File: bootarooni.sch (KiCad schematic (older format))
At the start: 25 parts, among them J1 USB_B_Micro, U1 74LS05, U2 Pico_USB, U3 ADUM3160, U4 74LCX541, U5 74AHCT1G125, U6 74LS299, U7 74LS299, U8 74LS299

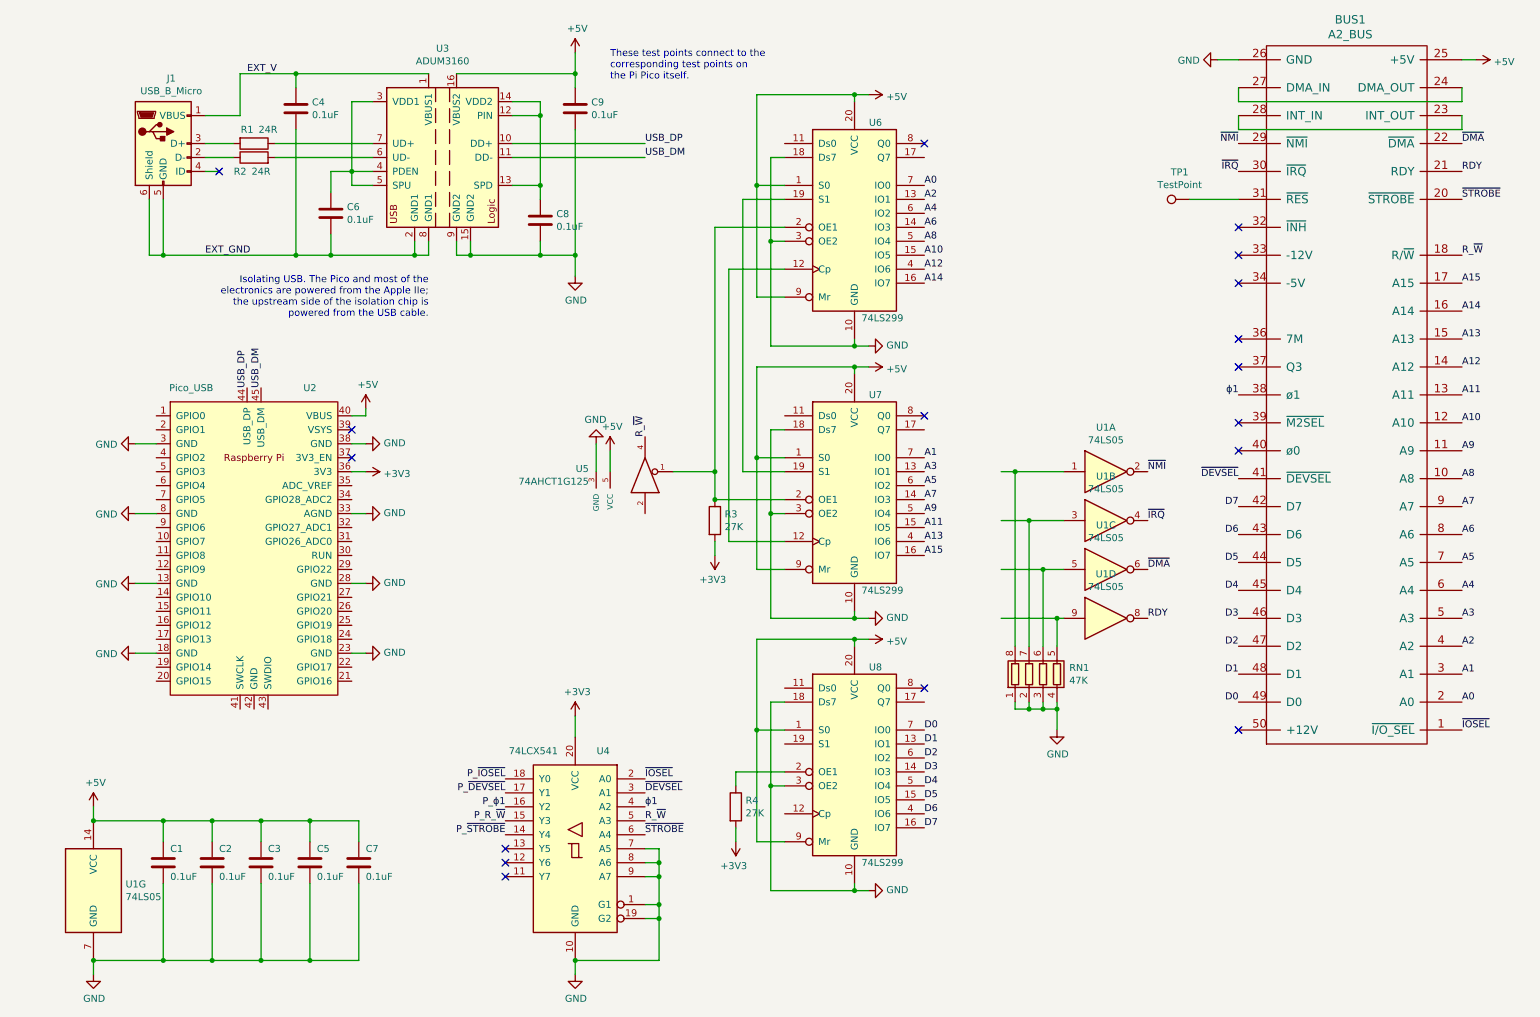
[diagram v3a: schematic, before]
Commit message: added LEDs, most layout done, need to reroute the power line
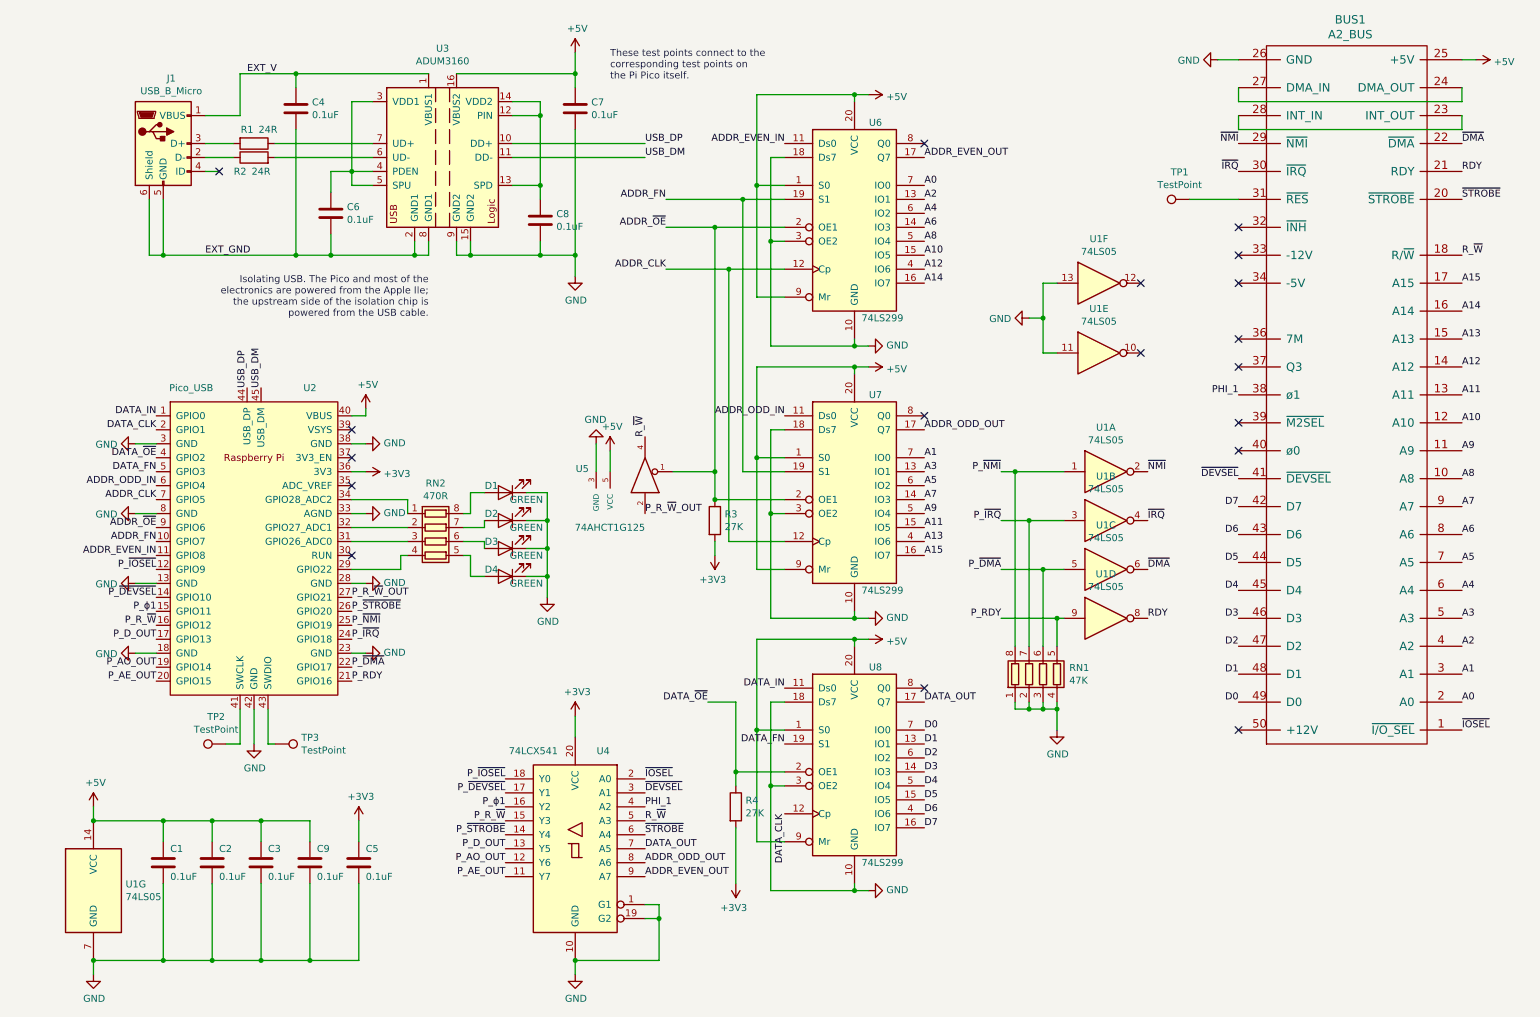
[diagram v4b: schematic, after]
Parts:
- added D1, D2, D3, D4: GREEN, LED_SMD:LED_0805_2012Metric, symbol Device:LED
- added RN2: 470R, bootarooni:SOIC-8, symbol Device:R_Pack04
- added TP2, TP3: TestPoint, TestPoint:TestPoint_Pad_D1.5mm, symbol Connector:TestPoint
- added unit 5 of U1
- added unit 6 of U1
- renumbered C9 to C7, C7 to C9
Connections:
- net +3V3: now also C5.2
- net +5V: no longer C5.2
- net GND: now also U2.42 (GND), D1.1 (K), D2.1 (K), D3.1 (K), D4.1 (K), U1.11, U1.13; no longer U4.7 (A5), U4.8 (A6), U4.9 (A7)
- net P_R_~W~: now also U2.16 (GPIO12)
- net P_~DEVSEL~: now also U2.14 (GPIO10)
- net P_~IOSEL~: now also U2.12 (GPIO9)
- net P_~STROBE~: now also U2.26 (GPIO20)
- net P_ϕ1: now also U2.15 (GPIO11)
- net ADDR_EVEN_IN: now reaches U6.11 (Ds0)
- net ADDR_EVEN_IN: now also U2.11 (GPIO8)
- net ADDR_CLK: now reaches U6.12 (Cp), U7.12 (Cp)
- net ADDR_CLK: now also U2.7 (GPIO5)
- net ADDR_EVEN_OUT: now reaches U6.17 (Q7)
- net ADDR_EVEN_OUT: now also U4.9 (A7)
- net ADDR_FN: now reaches U6.19 (S1), U7.19 (S1)
- net ADDR_FN: now also U2.10 (GPIO7)
- net ADDR_~OE~: now reaches R3.1, U5.1, U6.2 (OE1), U7.2 (OE1)
- net ADDR_~OE~: now also U2.9 (GPIO6)
- net P_AE_OUT: now reaches U4.11 (Y7)
- net P_AE_OUT: now also U2.20 (GPIO15)
- net P_AO_OUT: now reaches U4.12 (Y6)
- net P_AO_OUT: now also U2.19 (GPIO14)
- net P_D_OUT: now reaches U4.13 (Y5)
- net P_D_OUT: now also U2.17 (GPIO13)
- net P_R_~W~_OUT: now reaches U5.2
- net P_R_~W~_OUT: now also U2.27 (GPIO21)
- net ADDR_ODD_IN: now reaches U7.11 (Ds0)
- net ADDR_ODD_IN: now also U2.6 (GPIO4)
- net ADDR_ODD_OUT: now reaches U7.17 (Q7)
- net ADDR_ODD_OUT: now also U4.8 (A6)
- net DATA_IN: now reaches U8.11 (Ds0)
- net DATA_IN: now also U2.1 (GPIO0)
- net DATA_CLK: now reaches U8.12 (Cp)
- net DATA_CLK: now also U2.2 (GPIO1)
- net DATA_OUT: now reaches U8.17 (Q7)
- net DATA_OUT: now also U4.7 (A5)
- net DATA_FN: now reaches U8.19 (S1)
- net DATA_FN: now also U2.5 (GPIO3)
- net DATA_~OE~: now reaches R4.1, U8.2 (OE1)
- net DATA_~OE~: now also U2.4 (GPIO2)
- net P_RDY: now reaches U2.21 (GPIO16)
- net P_RDY: now also RN1.5 (R4.2), U1.9
- net P_~DMA~: now reaches U2.22 (GPIO17)
- net P_~DMA~: now also RN1.6 (R3.2), U1.5
- net P_~IRQ~: now reaches U2.24 (GPIO18)
- net P_~IRQ~: now also RN1.7 (R2.2), U1.3
- net P_~NMI~: now reaches U2.25 (GPIO19)
- net P_~NMI~: now also RN1.8 (R1.2), U1.1
- net at U2.29 (GPIO22): now also RN2.4 (R4.1)
- net at U2.31 (GPIO26_ADC0): now also RN2.3 (R3.1)
- net at U2.32 (GPIO27_ADC1): now also RN2.2 (R2.1)
- net at U2.34 (GPIO28_ADC2): now also RN2.1 (R1.1)
- net at U2.41 (SWCLK): now also TP2.1
- net at U2.43 (SWDIO): now also TP3.1
- net ϕ1 renamed PHI_1
- new net: D4.2 (A), RN2.5 (R4.2)
- new net: D3.2 (A), RN2.6 (R3.2)
- new net: D2.2 (A), RN2.7 (R2.2)
- new net: D1.2 (A), RN2.8 (R1.2)
- no-connect marks 17 -> 18
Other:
- moved on the sheet: C5, C9

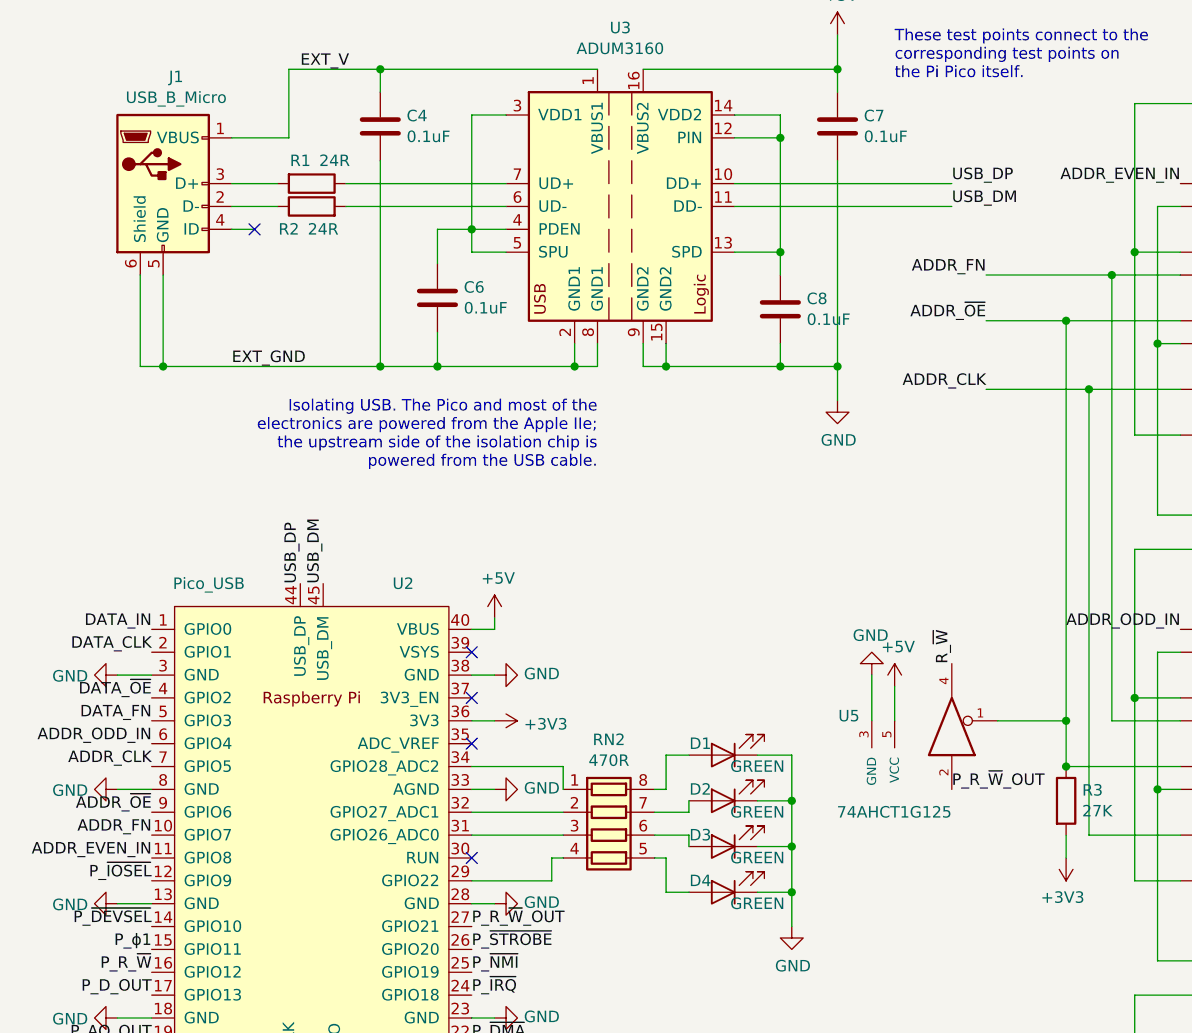
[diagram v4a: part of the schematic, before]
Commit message: initial layout done, needs board edge and mounting holes, along with verification
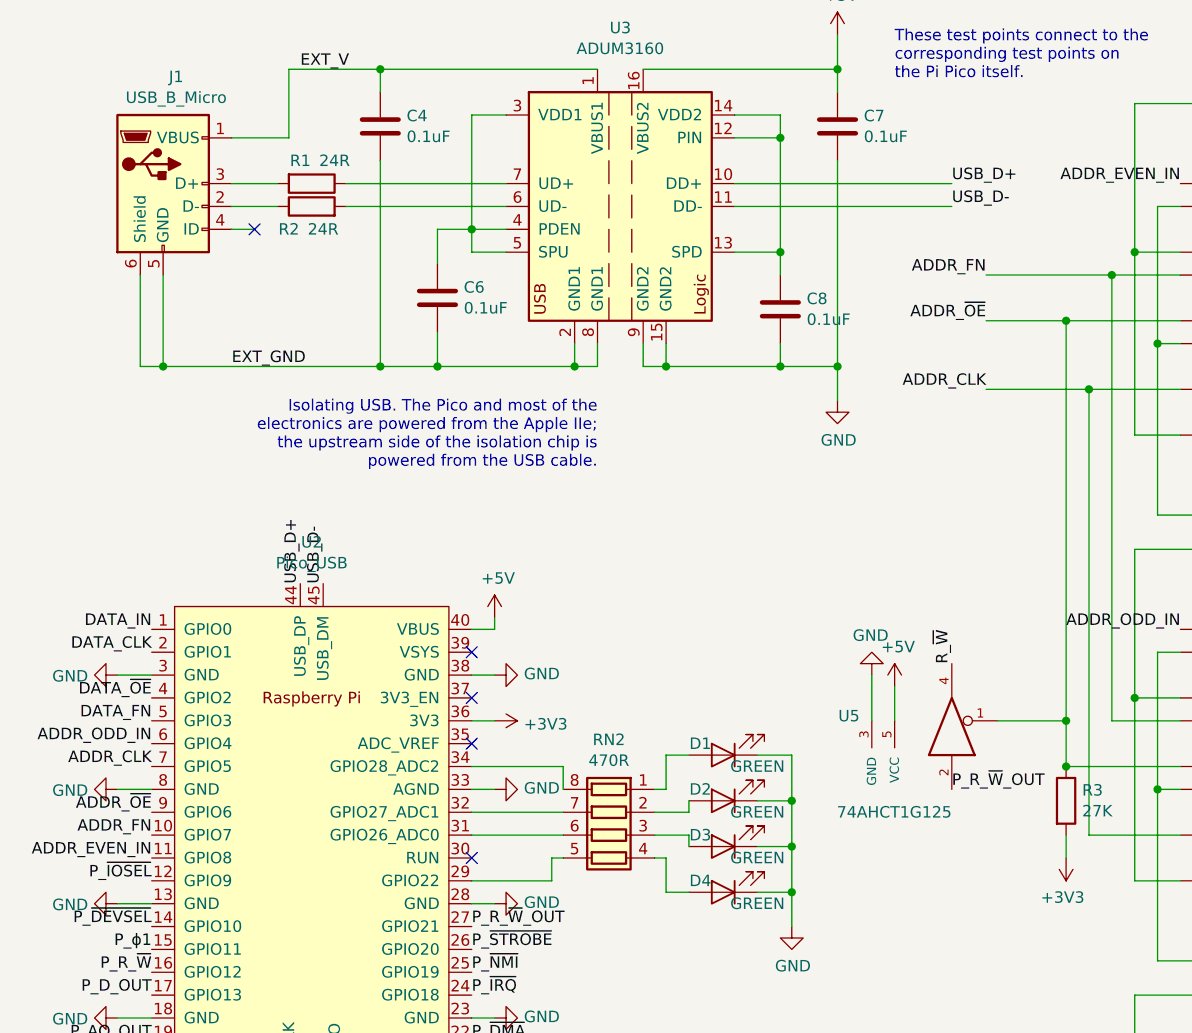
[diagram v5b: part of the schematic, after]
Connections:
- net at RN2.4 (R4.1): now also D4.2 (A); no longer U2.29 (GPIO22)
- net at RN2.3 (R3.1): now also D3.2 (A); no longer U2.31 (GPIO26_ADC0)
- net at RN2.2 (R2.1): now also D2.2 (A); no longer U2.32 (GPIO27_ADC1)
- net at RN2.1 (R1.1): now also D1.2 (A); no longer U2.34 (GPIO28_ADC2)
- net at RN2.5 (R4.2): now also U2.29 (GPIO22); no longer D4.2 (A)
- net at RN2.6 (R3.2): now also U2.31 (GPIO26_ADC0); no longer D3.2 (A)
- net at RN2.7 (R2.2): now also U2.32 (GPIO27_ADC1); no longer D2.2 (A)
- net at RN2.8 (R1.2): now also U2.34 (GPIO28_ADC2); no longer D1.2 (A)
- net USB_DM renamed USB_D-
- net USB_DP renamed USB_D+
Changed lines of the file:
@@
 NoConn ~ 1750 1750
 Text Label 4800 1550 0    50   ~ 0
-USB_DP
+USB_D+
 Text Label 4800 1650 0    50   ~ 0
-USB_DM
+USB_D-
 $Comp
 L power:GND #PWR0101
@@
 Wire Wire Line
 	8700 1950 9050 1950
-$Comp
-L MCU_RaspberryPi_and_Boards:Pico_USB U2
-U 1 1 6040CDC5
-P 2000 4450
-F 0 "U2" H 2400 5600 50  0000 C CNN
-F 1 "Pico_USB" H 1550 5600 50  0000 C CNN
-F 2 "MCU_RaspberryPi_and_Boards:RPi_Pico_USB_SMD_TH" V 2000 4450 50  0001 C CNN
-F 3 "" H 2000 4450 50  0001 C CNN
-	1    2000 4450
-	1    0    0    -1
-$EndComp
 Text Label 1950 3300 1    50   ~ 0
-USB_DP
+USB_D+
 Text Label 2050 3300 1    50   ~ 0
-USB_DM
+USB_D-
 Wire Wire Line
 	9050 1150 9050 1250
@@
 F 3 "~" H 3300 4400 50  0001 C CNN
 	1    3300 4400
-	0    1    1    0
+	0    -1   1    0
 $EndComp
 Wire Wire Line
@@
 	4100 4050 4100 4250
 Connection ~ 4100 4250
+$Comp
+L MCU_RaspberryPi_and_Boards:Pico_USB U2
+U 1 1 608C304D
+P 2000 4450
+F 0 "U2" H 2000 5781 50  0000 C CNN
+F 1 "Pico_USB" H 2000 5690 50  0000 C CNN
+F 2 "MCU_RaspberryPi_and_Boards:RPi_Pico_USB_SMD_TH" V 2000 4450 50  0001 C CNN
+F 3 "" H 2000 4450 50  0001 C CNN
+	1    2000 4450
+	1    0    0    -1
+$EndComp
 $EndSCHEMATC

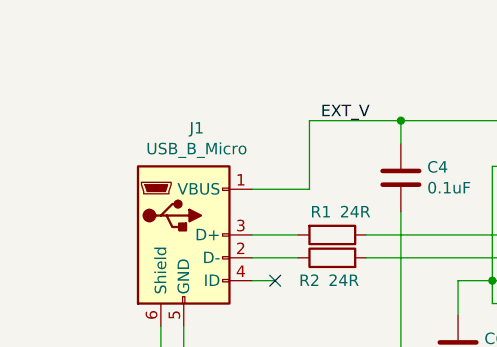
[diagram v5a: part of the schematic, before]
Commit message: added mounting holes, board outlines
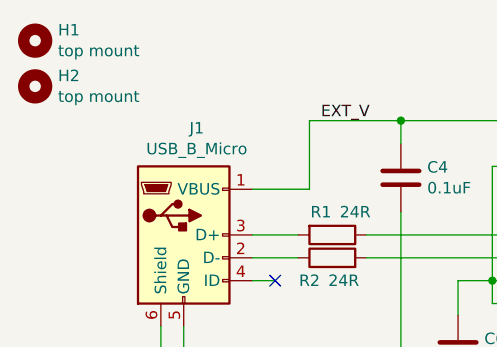
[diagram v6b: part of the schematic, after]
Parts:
- added H1, H2: top mount, MountingHole:MountingHole_3.2mm_M3, symbol Mechanical:MountingHole
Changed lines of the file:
@@
+	1    0    0    -1
+$EndComp
+$Comp
+L Mechanical:MountingHole H1
+U 1 1 6091C6CA
+P 700 700
+F 0 "H1" H 800 746 50  0000 L CNN
+F 1 "top mount" H 800 655 50  0000 L CNN
+F 2 "MountingHole:MountingHole_3.2mm_M3" H 700 700 50  0001 C CNN
+F 3 "~" H 700 700 50  0001 C CNN
+	1    700  700
+	1    0    0    -1
+$EndComp
+$Comp
+L Mechanical:MountingHole H2
+U 1 1 6091C9F0
+P 700 900
+F 0 "H2" H 800 946 50  0000 L CNN
+F 1 "top mount" H 800 855 50  0000 L CNN
+F 2 "MountingHole:MountingHole_3.2mm_M3" H 700 900 50  0001 C CNN
+F 3 "~" H 700 900 50  0001 C CNN
+	1    700  900
 	1    0    0    -1
 $EndComp
